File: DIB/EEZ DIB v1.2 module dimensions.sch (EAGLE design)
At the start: 4 parts, among them X1 77317-104-28LF, X2 ZL263-20DG

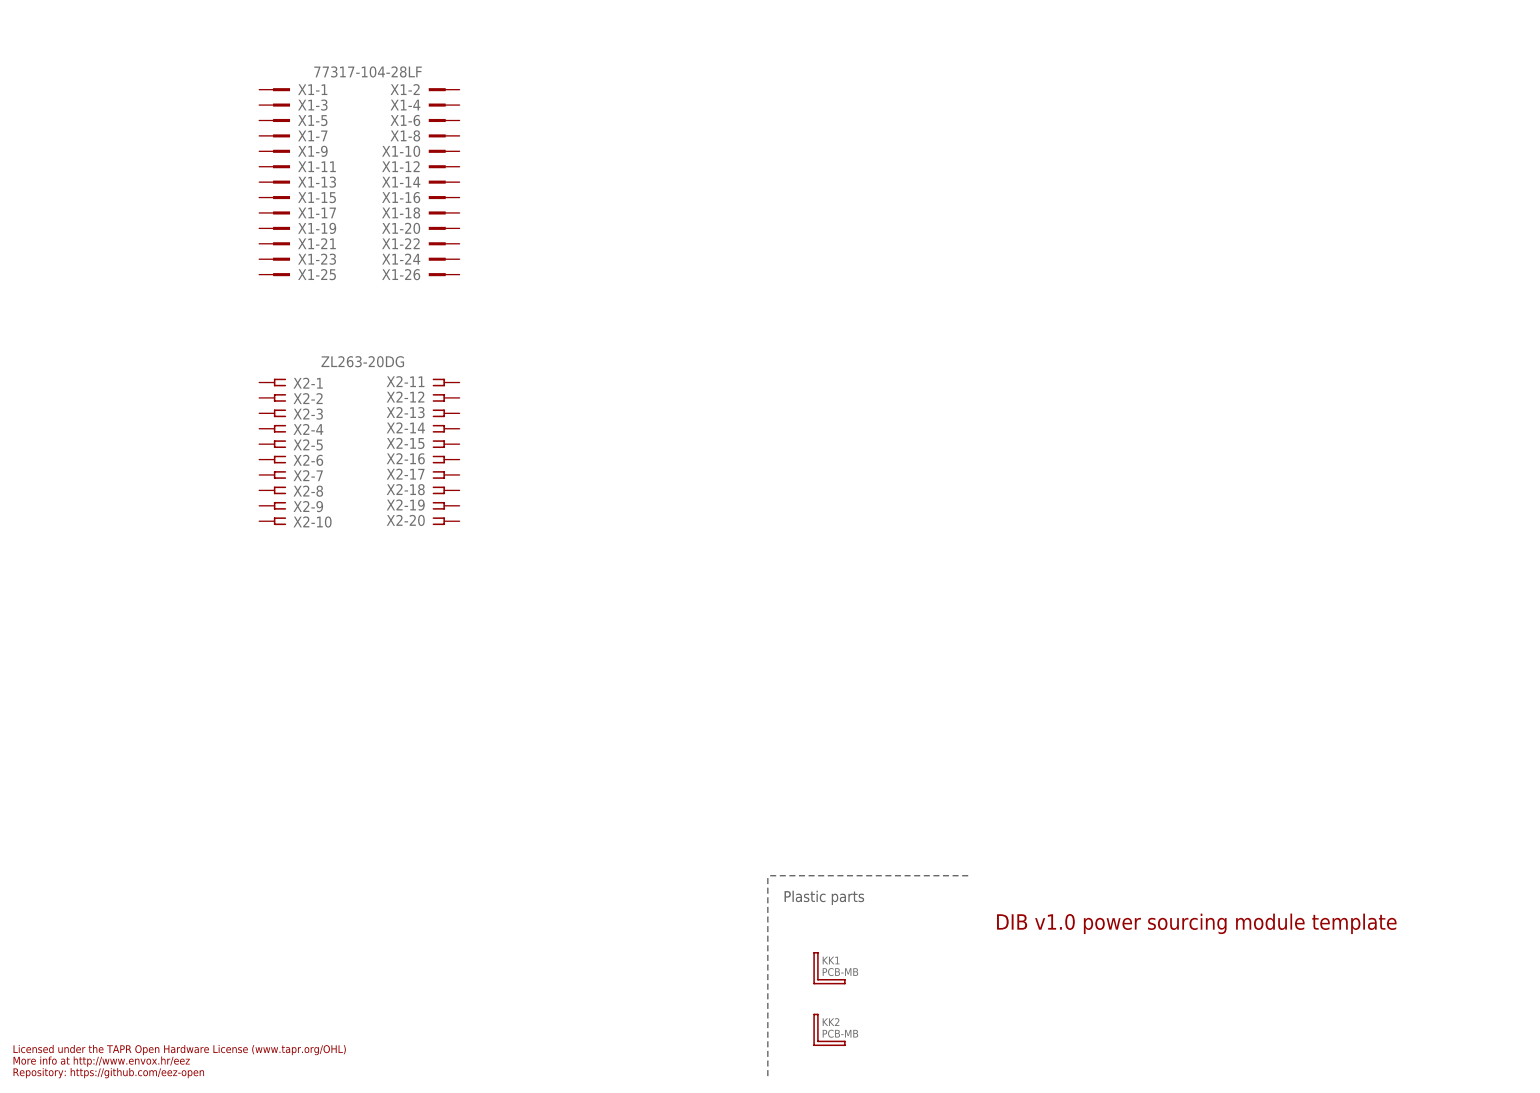
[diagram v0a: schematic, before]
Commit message: DIB v1.2 specification (ADIB added)
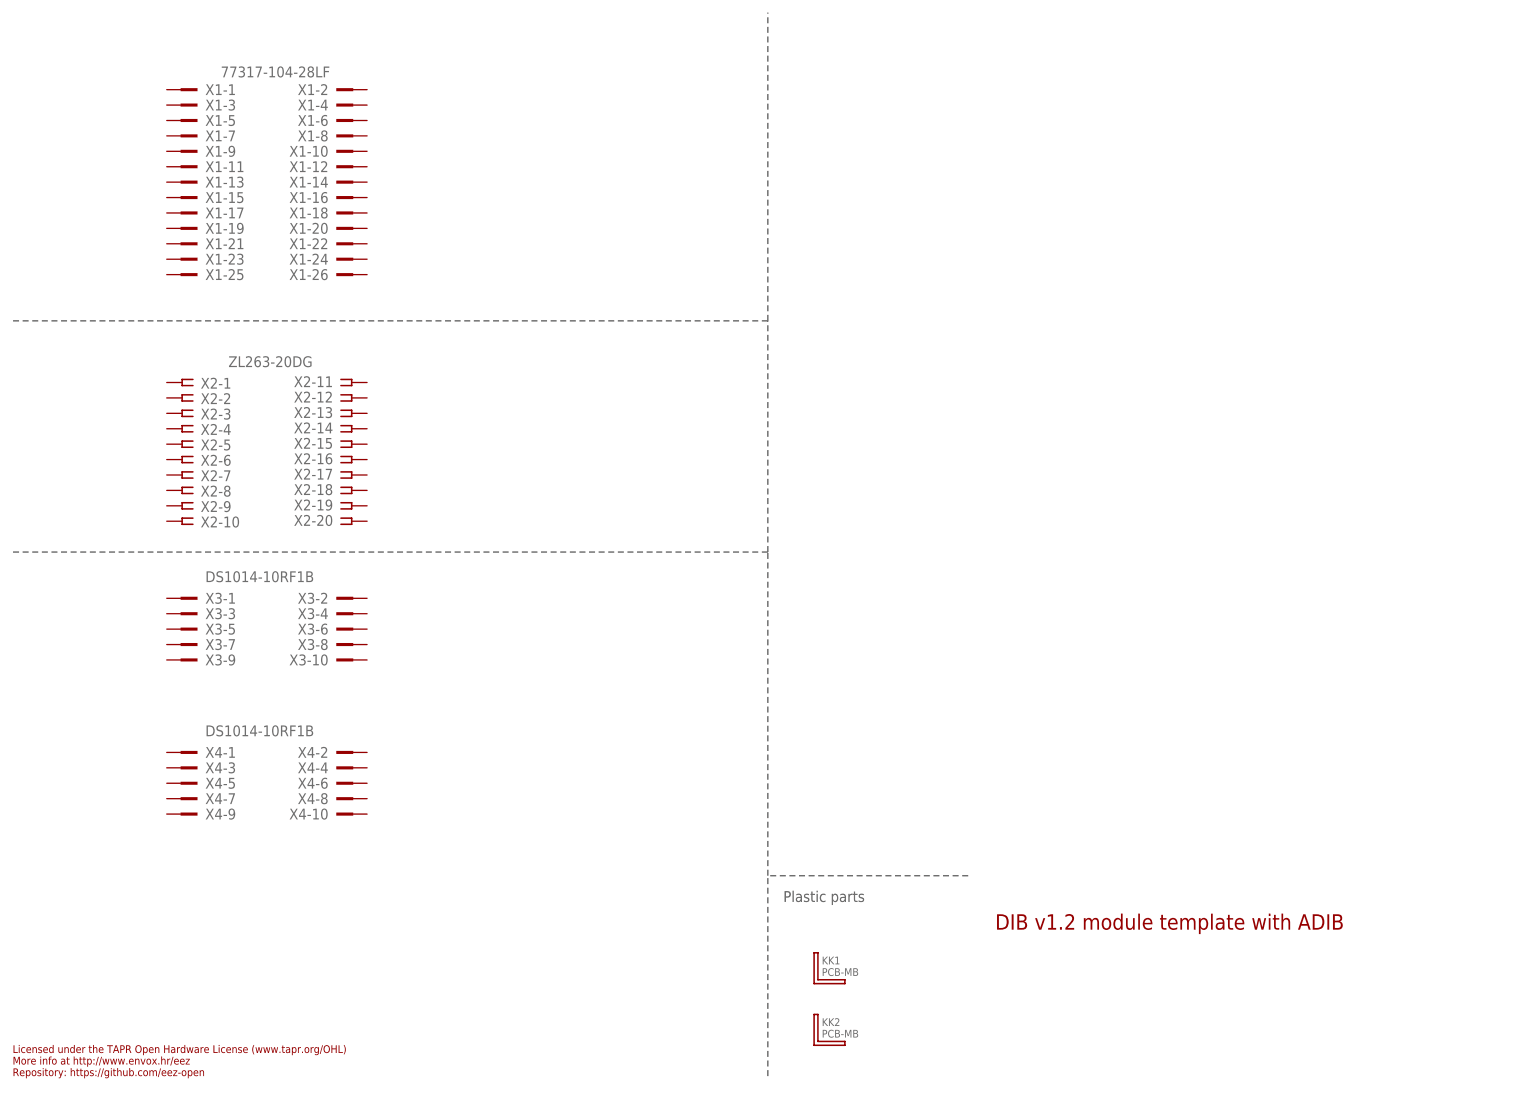
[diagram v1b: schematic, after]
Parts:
- added X3, X4: DS1014-10RF1B, EEZ_connectors:DS1014-10RF1B
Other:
- note added: "10 ID_Gnd"
- note added: "10-pin ADIB socket"
- note added: "2 Guard+"
- note added: "4 AIN+"
- note added: "6 Guard+"
- note added: "8 ADIB_ID2"
- note added: "ADIB_ID0 7"
- note added: "ADIB_ID1 9"
- note added: "AIN- 3"
- note added: "DIB v1.2 module template with ADIB"
- note added: "Guard- 1"
- note added: "Guard- 5"
- note removed: "DIB v1.0 power sourcing module template"
- moved on the sheet: X1-1, X1-10, X1-11, X1-12, X1-13, X1-14, X1-15, X1-16, X1-17, X1-18, X1-19, X1-2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
